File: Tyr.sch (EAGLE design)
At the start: 192 parts, among them J1 TYR_TYR_DISPLAY, U1 TYR_ATMEGA32U4, U2 CONTROLLER_PRTR5V0U2X, U4 TYR_TPS2552, X1 CONTROLLER_USB-C-12PUSB-C-12P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, Y1 16Mhz

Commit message: Initial
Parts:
- removed U1: TYR_ATMEGA32U4, Tyr:TYR_ATMEGA32U4
- added C45, C46: 22p, Tyr:COMPONENTS_CAPACITOR-0603
- added C47: 10n, Tyr:COMPONENTS_CAPACITOR-0603
- added C48: 1u, Tyr:COMPONENTS_CAPACITOR-0603
- added C49, C50, C51, C52, C54: 100n, Tyr:COMPONENTS_CAPACITOR-0603
- added C53: 4.7u, Tyr:COMPONENTS_CAPACITOR-0603
- added D42: 1N4148, Tyr:COMPONENTS_DIODE-SOD-123
- added D43: BAT60J, diode:BAT60J
- added U$1: STM32F303CC, Tyr:STM32F303CC
- added U$2: MCP1700T, Tyr:MCP1700T
- added Y2: 72Mhz, Tyr:CONTROLLER_CRYSTAL-4PIN-3.2X2.5
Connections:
- new net 3.3V: C47.1, C48.1, C50.1, C51.1, C52.1, C53.1, C54.2, D42.A, U$1.VBAT, U$1.VCC, U$1.VCC/VDDA/VREF+, U$1.VCC1, U$1.VCC2, U$2.VO
- new net BOOT0: U$1.BOOT0
- new net NRST: U$1.NRST
- net COLUMN0: no longer U1.PD4(ICP1/ADC8)
- net COLUMN1: no longer U1.PD6(T1/ADC9/!OC4D)
- net COLUMN2: no longer U1.PD7(OC4D/ADC10/T0)
- net COLUMN3: no longer U1.PB4(ADC11)
- net COLUMN4: no longer U1.PB5(OC1A/ADC12/!OC4B)
- net COLUMN5: no longer U1.PB6(OC1B/OC4B/ADC13)
- net COLUMN6: no longer U1.PC6(OC3A/!OC4A)
- net COLUMN7: no longer U1.PC7(ICP3/CLK0/OC4A)
- net D+: now also U$1.PA12/USB_DP; no longer U1.D+
- net D-: now also U$1.PA11/USB_DM; no longer U1.D-
- net GND: now also C45.1, C46.1, C47.2, C48.2, C49.1, C50.2, C51.2, C52.2, C53.2, C54.1, D43.A, U$1.GND, U$1.GND/VSSA/VREF-, U$1.GND1, U$1.GND2, U$2.GND, Y2.GND; no longer U1.GND, U1.GND1, U1.GND2, U1.GND3, U1.THERMAL, U1.UGND
- net LED_DATA: no longer U1.PD5(XCK/CTS)
- net LED_ENABLE: no longer U1.PD2(INT2/RXD1)
- net LED_FAULT: no longer U1.PD3(INT3/TXD1)
- net N$5: no longer U1.PE2(!HWB)
- net N$8: no longer U1.UCAP
- net RESET: no longer U1./RESET
- net ROW0: no longer U1.PF0(ADC0)
- net ROW1: no longer U1.PF1(ADC1)
- net ROW2: no longer U1.PF4(ADC4/TCK)
- net ROW3: no longer U1.PF5(ADC5/TMS)
- net ROW4: no longer U1.PF6(ADC6/TDO)
- net ROW5: no longer U1.PF7(ADC7(TDI)
- net SCL: now also U$1.I2C2_SCL/PA9; no longer U1.PD0(INT0/OC0B/SCL)
- net SDA: now also U$1.I2C2_SDA/PA10; no longer U1.PD1(INT1/SDA)
- net VCC: now also C49.2, D42.C, D43.C, U$2.VI; no longer U1.AVCC, U1.AVCC1, U1.UVCC, U1.VBUS, U1.VCC, U1.VCC1
- net XTAL1: now also C45.2, U$1.PF0/OSC_IN/12C2_SDA, Y2.1; no longer U1.XTAL1
- net XTAL2: now also C46.2, U$1.PF1/OSC_OUT/I2C2_SCL, Y2.2; no longer U1.XTAL2

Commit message: Layout
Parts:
- removed C3, C4: 0.1u, Tyr:COMPONENTS_CAPACITOR-0603
- removed C5: 4.7u, Tyr:COMPONENTS_CAPACITOR-0603
- removed C6, C7: 22p, Tyr:COMPONENTS_CAPACITOR-0603
- removed R3: 10k, Tyr:COMPONENTS_RESISTOR-0603
- removed Y1: 16Mhz, Tyr:CONTROLLER_CRYSTAL-4PIN-3.2X2.5
- added D45: 1N4148, Tyr:COMPONENTS_DIODE-SOD-123
- added U$3: DTC123J, Tyr:DTC123J
- C1: value 1u -> 4.7n
- C2: value 0.1u -> 10u
- R1: value 10k -> 100k
- Y2: value 72Mhz -> 8Mhz
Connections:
- removed net N$8: C1.2
- removed net RESET: R1.2, SJ1.2
- net 3.3V: now also SJ1.1
- net BOOT0: now also C2.2, D45.C, R1.1
- net GND: now also C1.2, R1.2, U$3.E; no longer C1.1, C3.1, C4.1, C5.1, C6.1, C7.1, R3.1, SJ1.1, Y1.GND
- net N$5: now also D45.A, SJ1.2, U$3.B; no longer R3.2
- net NRST: now also C1.1, U$3.C
- net VCC: no longer C2.2, C3.2, C4.2, C5.2, R1.1
- net XTAL1: no longer C6.2, Y1.1
- net XTAL2: no longer C7.2, Y1.2

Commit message: Update
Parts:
- removed 1, 2, 3, 4, 5, 6, A, ALT, B, C, CTRL, D, E, ESC, F, F1, F2, F3, F4, F5, F6, FN, G, GRAVE, H, HOME, INSERT, Q, R, S, T, TAB, V, W, WIN, X, Y, Z: KEYBOARD_KEYSWITCH-MX-1U-HOTSWAP, Tyr:KEYBOARD_KEYSWITCH-MX-1U-HOTSWAP
- removed C50, C51, C52, C54: 100n, Tyr:COMPONENTS_CAPACITOR-0603
- removed C53: 4.7u, Tyr:COMPONENTS_CAPACITOR-0603
- removed CAPSLOCK: KEYBOARD_KEYSWITCH-MX-1U-HOTSWAPCAPSLOCK, Tyr:KEYBOARD_KEYSWITCH-MX-1U-HOTSWAPCAPSLOCK
- removed D45: 1N4148, Tyr:COMPONENTS_DIODE-SOD-123
- removed R10: 5.1k, Tyr:COMPONENTS_RESISTOR-0603
- removed SHIFT, SPACE: KEYBOARD_KEYSWITCH-MX-2U-HOTSWAP, Tyr:KEYBOARD_KEYSWITCH-MX-2U-HOTSWAP
- removed SJ1: (no value), Tyr:MICROBUILDER_SOLDERJUMPER
- removed U$3: DTC123J, Tyr:DTC123J
- removed Y2: 8Mhz, Tyr:CONTROLLER_CRYSTAL-4PIN-3.2X2.5
- added C3: 4.7n, Tyr:COMPONENTS_CAPACITOR-0603
- added C4: 10u, Tyr:COMPONENTS_CAPACITOR-0603
- added C5: 22p, Tyr:COMPONENTS_CAPACITOR-0603
- added C6: 0.1u, Tyr:COMPONENTS_CAPACITOR-0603
- added C7: 10n, Tyr:COMPONENTS_CAPACITOR-0603
- added D44: 1N4148, Tyr:COMPONENTS_DIODE-SOD-123
- added KEYSWITCH1, KEYSWITCH10, KEYSWITCH11, KEYSWITCH12, KEYSWITCH13, KEYSWITCH14, KEYSWITCH15, KEYSWITCH16, KEYSWITCH17, KEYSWITCH18, KEYSWITCH19, KEYSWITCH2, KEYSWITCH20, KEYSWITCH21, KEYSWITCH22, KEYSWITCH23, KEYSWITCH24, KEYSWITCH25, KEYSWITCH26, KEYSWITCH27, KEYSWITCH28, KEYSWITCH29, KEYSWITCH3, KEYSWITCH30, KEYSWITCH31, KEYSWITCH32, KEYSWITCH33, KEYSWITCH34, KEYSWITCH35, KEYSWITCH36, KEYSWITCH37, KEYSWITCH38, KEYSWITCH39, KEYSWITCH5, KEYSWITCH6, KEYSWITCH7, KEYSWITCH8, KEYSWITCH9: KEYBOARD_KEYSWITCH-MX-1U-HOTSWAP, Tyr:KEYBOARD_KEYSWITCH-MX-1U-HOTSWAP
- added KEYSWITCH4: KEYBOARD_KEYSWITCH-MX-1U-HOTSWAPCAPSLOCK, Tyr:KEYBOARD_KEYSWITCH-MX-1U-HOTSWAPCAPSLOCK
- added Q1: DTC123J, Tyr:DTC123J
- added R3: 100k, Tyr:COMPONENTS_RESISTOR-0603
- added SWITCH1, SWITCH2: KEYBOARD_KEYSWITCH-MX-2U-HOTSWAP, Tyr:KEYBOARD_KEYSWITCH-MX-2U-HOTSWAP
- added U1: (no value), Tyr:MICROBUILDER_INA219
- added U5: MCP1700T, Tyr:MCP1700T
- added Y1: 8Mhz, Tyr:CONTROLLER_CRYSTAL-4PIN-3.2X2.5
- C1: value 4.7n -> 0.1u
- C10, C11, C13, C14: value 104 -> 100n
- C12: value 104 -> 4.7u
- C2: value 10u -> 22p
- C45, C46: value 22p -> 104
- C47: value 10n -> 104
- C48: value 1u -> 104
- C49: value 100n -> 104
- C8: value 0.1u -> 1u
- C9: value 0.1u -> 100n
- D2: value 1N4148 -> BAT60J; device Tyr:COMPONENTS_DIODE-SOD-123 -> diode:BAT60J
- D43: value BAT60J -> 1N4148; device diode:BAT60J -> Tyr:COMPONENTS_DIODE-SOD-123
- R2: value 22 -> 0.1/1% (PT2512FK-070R1L); device Tyr:COMPONENTS_RESISTOR-0603 -> Tyr:MICROBUILDER_RESISTOR2512
- R4: value 22 -> 10k
- R5: value 0.1/1% (PT2512FK-070R1L) -> 54.9k; device Tyr:MICROBUILDER_RESISTOR2512 -> Tyr:COMPONENTS_RESISTOR-0603
- R6: value 54.9k -> 22
- R7: value 10k -> 22
- R8: value 100k -> 5.1k
- U$1: value STM32F303CC -> BUTTON; device Tyr:STM32F303CC -> Tyr:BUTTON
- U$2: value MCP1700T -> PINHEADER_1X6; device Tyr:MCP1700T -> Tyr:PINHEADER_1X6
- U2: value CONTROLLER_PRTR5V0U2X -> STM32F303CC; device Tyr:CONTROLLER_PRTR5V0U2X -> Tyr:STM32F303CC
- U3: value (none) -> TYR_TPS2552; device Tyr:MICROBUILDER_INA219 -> Tyr:TYR_TPS2552
- U4: value TYR_TPS2552 -> CONTROLLER_PRTR5V0U2X; device Tyr:TYR_TPS2552 -> Tyr:CONTROLLER_PRTR5V0U2X
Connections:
- new net SWCLK: U$2.5, U2.PA14/SWCLK-JTCK/I2C1_SDA
- new net SWDIO: U$2.4, U2.PA13/SWDIO-JTMS
- net 3.3V: now also C10.1, C11.1, C12.1, C14.2, C7.1, C8.1, C9.1, D3.A, J1.4, U$1.P$2, U$2.6, U2.VBAT, U2.VCC, U2.VCC/VDDA/VREF+, U2.VCC1, U2.VCC2, U5.VO; no longer C47.1, C48.1, C50.1, C51.1, C52.1, C53.1, C54.2, D42.A, SJ1.1, U$1.VBAT, U$1.VCC, U$1.VCC/VDDA/VREF+, U$1.VCC1, U$1.VCC2, U$2.VO
- net BOOT0: now also C4.2, D1.C, U$2.3, U2.BOOT0; no longer C2.2, D45.C, U$1.BOOT0
- net COLUMN0: now also KEYSWITCH1.P1, KEYSWITCH2.P1, KEYSWITCH3.P1, KEYSWITCH4.P1, KEYSWITCH5.P1, SWITCH1.P1, U2.DAC1-OUT2/PA5; no longer CAPSLOCK.P1, CTRL.P1, ESC.P1, GRAVE.P1, SHIFT.P1, TAB.P1
- net COLUMN1: now also KEYSWITCH10.P1, KEYSWITCH11.P1, KEYSWITCH6.P1, KEYSWITCH7.P1, KEYSWITCH8.P1, KEYSWITCH9.P1, U2.PA6; no longer 1.P1, A.P1, F1.P1, Q.P1, WIN.P1, Z.P1
- net COLUMN2: now also KEYSWITCH12.P1, KEYSWITCH13.P1, KEYSWITCH14.P1, KEYSWITCH15.P1, KEYSWITCH16.P1, KEYSWITCH17.P1, U2.PA7; no longer 2.P1, ALT.P1, F2.P1, S.P1, W.P1, X.P1
- net COLUMN3: now also KEYSWITCH18.P1, KEYSWITCH19.P1, KEYSWITCH20.P1, KEYSWITCH21.P1, KEYSWITCH22.P1, SWITCH2.P1, U2.PB0; no longer 3.P1, C.P1, D.P1, E.P1, F3.P1, SPACE.P1
- net COLUMN4: now also KEYSWITCH23.P1, KEYSWITCH24.P1, KEYSWITCH25.P1, KEYSWITCH26.P1, KEYSWITCH27.P1, U2.PB1; no longer 4.P1, F.P1, F4.P1, R.P1, V.P1
- net COLUMN5: now also KEYSWITCH28.P1, KEYSWITCH29.P1, KEYSWITCH30.P1, KEYSWITCH31.P1, KEYSWITCH32.P1, KEYSWITCH33.P1, U2.PB10; no longer 5.P1, B.P1, F5.P1, FN.P1, G.P1, T.P1
- net COLUMN6: now also KEYSWITCH34.P1, KEYSWITCH35.P1, U2.PB11; no longer 6.P1, F6.P1
- net COLUMN7: now also KEYSWITCH36.P1, KEYSWITCH37.P1, KEYSWITCH38.P1, KEYSWITCH39.P1, U2.PB12; no longer H.P1, HOME.P1, INSERT.P1, Y.P1
- net D+: now also R7.2, U2.PA12/USB_DP; no longer R4.2, U$1.PA12/USB_DP
- net D-: now also R6.2, U2.PA11/USB_DM; no longer R2.2, U$1.PA11/USB_DM
- net GND: now also C1.1, C10.2, C11.2, C12.2, C3.2, C4.1, C47.1, C48.1, C5.1, C6.1, C7.2, C8.2, C9.2, D2.A, KEYSWITCH1.HOLE, KEYSWITCH10.HOLE, KEYSWITCH11.HOLE, KEYSWITCH12.HOLE, KEYSWITCH13.HOLE, KEYSWITCH14.HOLE, KEYSWITCH15.HOLE, KEYSWITCH16.HOLE, KEYSWITCH17.HOLE, KEYSWITCH18.HOLE, KEYSWITCH19.HOLE, KEYSWITCH2.HOLE, KEYSWITCH20.HOLE, KEYSWITCH21.HOLE, KEYSWITCH22.HOLE, KEYSWITCH23.HOLE, KEYSWITCH24.HOLE, KEYSWITCH25.HOLE, KEYSWITCH26.HOLE, KEYSWITCH27.HOLE, KEYSWITCH28.HOLE, KEYSWITCH29.HOLE, KEYSWITCH3.HOLE, KEYSWITCH30.HOLE, KEYSWITCH31.HOLE, KEYSWITCH32.HOLE, KEYSWITCH33.HOLE, KEYSWITCH34.HOLE, KEYSWITCH35.HOLE, KEYSWITCH36.HOLE, KEYSWITCH37.HOLE, KEYSWITCH38.HOLE, KEYSWITCH39.HOLE, KEYSWITCH4.HOLE, KEYSWITCH5.HOLE, KEYSWITCH6.HOLE, KEYSWITCH7.HOLE, KEYSWITCH8.HOLE, KEYSWITCH9.HOLE, Q1.E, R4.1, R5.1, R8.2, SWITCH1.HOLE, SWITCH2.HOLE, U$2.1, U1.GND, U2.GND, U2.GND/VSSA/VREF-, U2.GND1, U2.GND2, U4.1, U5.GND, Y1.GND; no longer 1.HOLE, 2.HOLE, 3.HOLE, 4.HOLE, 5.HOLE, 6.HOLE, A.HOLE, ALT.HOLE, B.HOLE, C.HOLE, C1.2, C10.1, C11.1, C12.1, C47.2, C48.2, C50.2, C51.2, C52.2, C53.2, C54.1, C8.1, C9.1, CAPSLOCK.HOLE, CTRL.HOLE, D.HOLE, D43.A, E.HOLE, ESC.HOLE, F.HOLE, F1.HOLE, F2.HOLE, F3.HOLE, F4.HOLE, F5.HOLE, F6.HOLE, FN.HOLE, G.HOLE, GRAVE.HOLE, H.HOLE, HOME.HOLE, INSERT.HOLE, Q.HOLE, R.HOLE, R10.2, R6.1, R7.1, S.HOLE, SHIFT.HOLE, SPACE.HOLE, T.HOLE, TAB.HOLE, U$1.GND, U$1.GND/VSSA/VREF-, U$1.GND1, U$1.GND2, U$2.GND, U$3.E, U2.1, U4.GND, V.HOLE, W.HOLE, WIN.HOLE, X.HOLE, Y.HOLE, Y2.GND, Z.HOLE
- net LED_DATA: now also LED35.DI, U2.DAC1-OUT1/PA4; no longer LED41.DI
- net LED_ENABLE: now also R4.2, U2.PA1, U3.EN; no longer R7.2, U4.EN
- net LED_FAULT: now also R3.1, U2.PA2, U3.FAULT; no longer R8.1, U4.FAULT
- net LED_VCC: now also C45.2, C46.2, C47.2, C48.2, C49.2, U3.OUT; no longer C10.2, C11.2, C12.2, C13.2, C14.2, U4.OUT
- net N$1: now also D11.A, KEYSWITCH7.P0; no longer 1.P0, D10.A
- net N$10: now also D4.A, KEYSWITCH1.P0; no longer D1.A, ESC.P0
- net N$11: now also D10.A, KEYSWITCH6.P0; no longer D2.A, F1.P0
- net N$12: now also D16.A, KEYSWITCH12.P0; no longer D3.A, F2.P0
- net N$13: now also D22.A, KEYSWITCH18.P0; no longer D4.A, F3.P0
- net N$14: now also D28.A, KEYSWITCH23.P0; no longer D5.A, F4.P0
- net N$15: now also D33.A, KEYSWITCH28.P0; no longer D6.A, F5.P0
- net N$16: now also D39.A, KEYSWITCH34.P0; no longer D7.A, F6.P0
- net N$17: now also D41.A, KEYSWITCH36.P0; no longer D8.A, HOME.P0
- net N$18: now also D42.A, KEYSWITCH37.P0; no longer D16.A, INSERT.P0
- net N$19: now also D40.A, KEYSWITCH35.P0; no longer 6.P0, D15.A
- net N$2: now also R2.2, U1.VIN-, U3.IN; no longer R5.2, U3.VIN-, U4.IN
- net N$20: now also D34.A, KEYSWITCH29.P0; no longer 5.P0, D14.A
- net N$21: now also D29.A, KEYSWITCH24.P0; no longer 4.P0, D13.A
- net N$22: now also D23.A, KEYSWITCH19.P0; no longer 3.P0, D12.A
- net N$23: now also D17.A, KEYSWITCH13.P0; no longer 2.P0, D11.A
- net N$24: now also D5.A, KEYSWITCH2.P0; no longer D9.A, GRAVE.P0
- net N$25: now also D43.A, KEYSWITCH38.P0; no longer D23.A, Y.P0
- net N$26: now also D35.A, KEYSWITCH30.P0; no longer D22.A, T.P0
- net N$27: now also D30.A, KEYSWITCH25.P0; no longer D21.A, R.P0
- net N$28: now also D24.A, KEYSWITCH20.P0; no longer D20.A, E.P0
- net N$29: now also D18.A, KEYSWITCH14.P0; no longer D19.A, W.P0
- net N$3: now also R5.2, U3.ILIM; no longer R6.2, U4.ILIM
- net N$30: now also LED18.DI, LED24.DO; no longer LED39.DI, LED40.DO
- net N$31: now also D6.A, KEYSWITCH3.P0; no longer D17.A, TAB.P0
- net N$32: now also D7.A, KEYSWITCH4.P0; no longer CAPSLOCK.P0, D24.A
- net N$33: now also D13.A, KEYSWITCH9.P0; no longer A.P0, D25.A
- net N$34: now also D19.A, KEYSWITCH15.P0; no longer D26.A, S.P0
- net N$35: now also D25.A, KEYSWITCH21.P0; no longer D.P0, D27.A
- net N$36: now also D31.A, KEYSWITCH26.P0; no longer D28.A, F.P0
- net N$37: now also D36.A, KEYSWITCH31.P0; no longer D29.A, G.P0
- net N$38: now also D44.A, KEYSWITCH39.P0; no longer D30.A, H.P0
- net N$39: now also D37.A, KEYSWITCH32.P0; no longer B.P0, D36.A
- net N$4: now also R8.1; no longer R9.1
- net N$40: now also D26.A, KEYSWITCH22.P0; no longer C.P0, D34.A
- net N$41: now also D20.A, KEYSWITCH16.P0; no longer D33.A, X.P0
- net N$42: now also D14.A, KEYSWITCH10.P0; no longer D32.A, Z.P0
- net N$43: now also D8.A, SWITCH1.P0; no longer D31.A, SHIFT.P0
- net N$44: now also D9.A, KEYSWITCH5.P0; no longer CTRL.P0, D37.A
- net N$45: now also D15.A, KEYSWITCH11.P0; no longer D38.A, WIN.P0
- net N$46: now also D21.A, KEYSWITCH17.P0; no longer ALT.P0, D39.A
- net N$47: now also D27.A, SWITCH2.P0; no longer D40.A, SPACE.P0
- net N$48: now also D38.A, KEYSWITCH33.P0; no longer D41.A, FN.P0
- net N$49: now also D32.A, KEYSWITCH27.P0; no longer D35.A, V.P0
- net N$5: now also D1.A, Q1.B, U$1.P$1; no longer D45.A, SJ1.2, U$3.B
- net N$50: now also D12.A, KEYSWITCH8.P0; no longer D18.A, Q.P0
- net N$51: now also LED12.DI, LED18.DO; no longer LED38.DI, LED39.DO
- net N$52: now also LED12.DO, LED6.DI; no longer LED37.DI, LED38.DO
- net N$53: now also LED34.DI, LED6.DO; no longer LED36.DI, LED37.DO
- net N$54: now also LED29.DI, LED34.DO; no longer LED35.DI, LED36.DO
- net N$55: now also LED23.DI, LED29.DO; no longer LED34.DI, LED35.DO
- net N$56: now also LED17.DI, LED23.DO; no longer LED33.DI, LED34.DO
- net N$57: now also LED11.DI, LED17.DO; no longer LED32.DI, LED33.DO
- net N$58: now also LED11.DO, LED5.DI; no longer LED31.DI, LED32.DO
- net N$59: now also LED41.DI, LED5.DO; no longer LED30.DI, LED31.DO
- net N$6: now also R6.1, U4.3; no longer R2.1, U2.3
- net N$60: now also LED33.DI, LED41.DO; no longer LED29.DI, LED30.DO
- net N$61: now also LED33.DO; no longer LED29.DO
- net N$62: now also LED22.DI; no longer LED27.DI
- net N$63: now also LED16.DI, LED22.DO; no longer LED26.DI, LED27.DO
- net N$64: now also LED10.DI, LED16.DO; no longer LED25.DI, LED26.DO
- net N$65: now also LED10.DO, LED4.DI; no longer LED24.DI, LED25.DO
- net N$66: now also LED4.DO, LED40.DI; no longer LED23.DI, LED24.DO
- net N$67: now also LED32.DI, LED40.DO; no longer LED22.DI, LED23.DO
- net N$68: now also LED27.DI, LED32.DO; no longer LED21.DI, LED22.DO
- net N$69: now also LED21.DI, LED27.DO; no longer LED20.DI, LED21.DO
- net N$7: now also R7.1, U4.2; no longer R4.1, U2.2
- net N$70: now also LED15.DI, LED21.DO; no longer LED19.DI, LED20.DO
- net N$71: now also LED15.DO, LED9.DI; no longer LED18.DI, LED19.DO
- net N$72: now also LED3.DI, LED9.DO; no longer LED17.DI, LED18.DO
- net N$73: now also LED3.DO, LED39.DI; no longer LED16.DI, LED17.DO
- net N$74: now also LED37.DI, LED39.DO; no longer LED15.DI, LED16.DO
- net N$75: now also LED31.DI, LED37.DO; no longer LED14.DI, LED15.DO
- net N$76: now also LED26.DI, LED31.DO; no longer LED13.DI, LED14.DO
- net N$77: now also LED20.DI, LED26.DO; no longer LED12.DI, LED13.DO
- net N$78: now also LED14.DI, LED20.DO; no longer LED11.DI, LED12.DO
- net N$79: now also LED14.DO, LED8.DI; no longer LED10.DI, LED11.DO
- net N$80: now also LED2.DI, LED8.DO; no longer LED10.DO, LED9.DI
- net N$81: now also LED2.DO, LED38.DI; no longer LED8.DI, LED9.DO
- net N$82: now also LED36.DI, LED38.DO; no longer LED7.DI, LED8.DO
- net N$83: now also LED30.DI, LED36.DO; no longer LED6.DI, LED7.DO
- net N$84: now also LED25.DI, LED30.DO; no longer LED5.DI, LED6.DO
- net N$85: now also LED19.DI, LED25.DO; no longer LED4.DI, LED5.DO
- net N$86: now also LED13.DI, LED19.DO; no longer LED3.DI, LED4.DO
- net N$87: now also LED13.DO, LED7.DI; no longer LED2.DI, LED3.DO
- net N$88: now also LED7.DO; no longer LED2.DO
- net N$89: now also R9.1; no longer R10.1
- net N$9: now also LED24.DI, LED35.DO; no longer LED40.DI, LED41.DO
- net NRST: now also C3.1, Q1.C, U$2.2, U2.NRST; no longer C1.1, U$1.NRST, U$3.C
- net ROW0: now also D10.C, D16.C, D22.C, D28.C, D33.C, D39.C, D41.C, U2.PA8; no longer D1.C, D2.C, D3.C, D5.C, D6.C, D7.C, D8.C
- net ROW1: now also D17.C, D23.C, D29.C, D34.C, D40.C, D42.C, D5.C, U2.PB15; no longer D10.C, D12.C, D13.C, D14.C, D15.C, D16.C, D9.C
- net ROW2: now also D12.C, D24.C, D30.C, D35.C, D43.C, D6.C, U2.PB14; no longer D17.C, D19.C, D20.C, D21.C, D22.C, D23.C
- net ROW3: now also D13.C, D19.C, D31.C, D36.C, D44.C, D7.C, U2.PB13; no longer D24.C, D26.C, D27.C, D28.C, D29.C, D30.C
- net ROW4: now also D14.C, D20.C, D26.C, D37.C, D8.C, U2.PB2; no longer D31.C, D33.C, D34.C, D35.C, D36.C
- net ROW5: now also D15.C, D21.C, D27.C, D9.C, U2.PA3; no longer D37.C, D39.C, D40.C, D41.C
- net SCL: now also U1.SCL, U2.I2C2_SCL/PA9; no longer U$1.I2C2_SCL/PA9, U3.SCL
- net SDA: now also U1.SDA, U2.I2C2_SDA/PA10; no longer U$1.I2C2_SDA/PA10, U3.SDA
- net VCC: now also C1.2, C13.2, C6.2, D2.C, D3.C, R2.1, R3.2, U1.VCC, U1.VIN+, U4.4, U5.VI; no longer C49.2, C8.2, C9.2, D42.C, D43.C, J1.4, R5.1, R8.2, U$2.VI, U2.4, U3.VCC, U3.VIN+
- net XTAL1: now also C2.2, U2.PF0/OSC_IN/12C2_SDA, Y1.1; no longer C45.2, U$1.PF0/OSC_IN/12C2_SDA, Y2.1
- net XTAL2: now also C5.2, U2.PF1/OSC_OUT/I2C2_SCL, Y1.2; no longer C46.2, U$1.PF1/OSC_OUT/I2C2_SCL, Y2.2

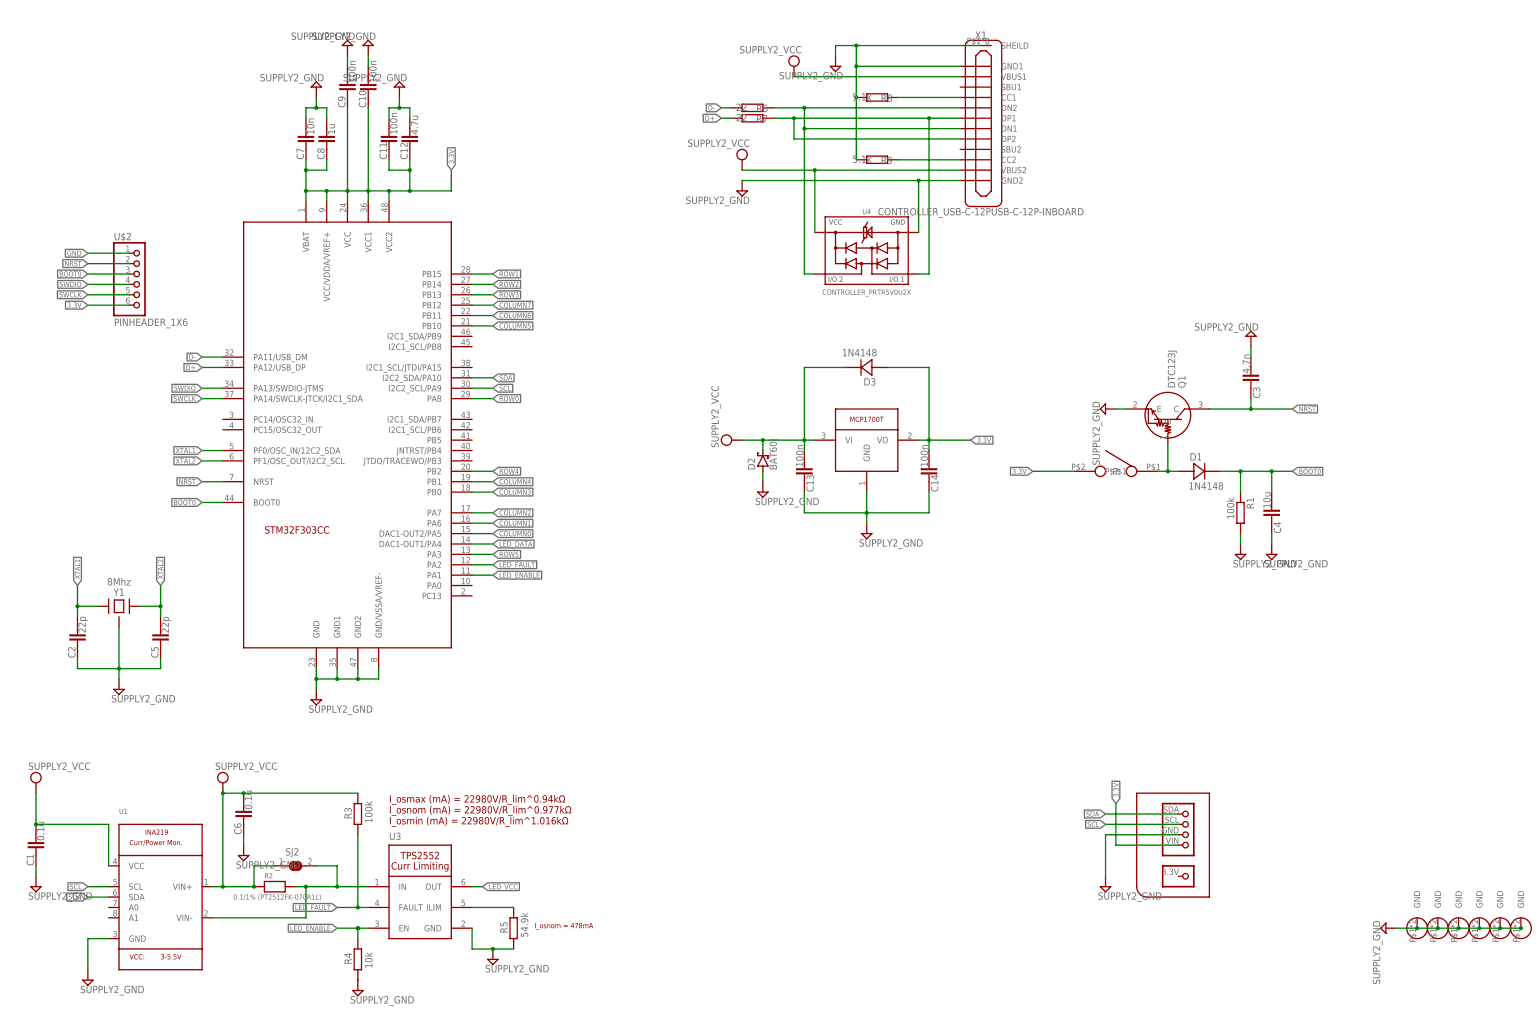
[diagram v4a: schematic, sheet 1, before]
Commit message: Fix current monitoring & added I2C FRAM
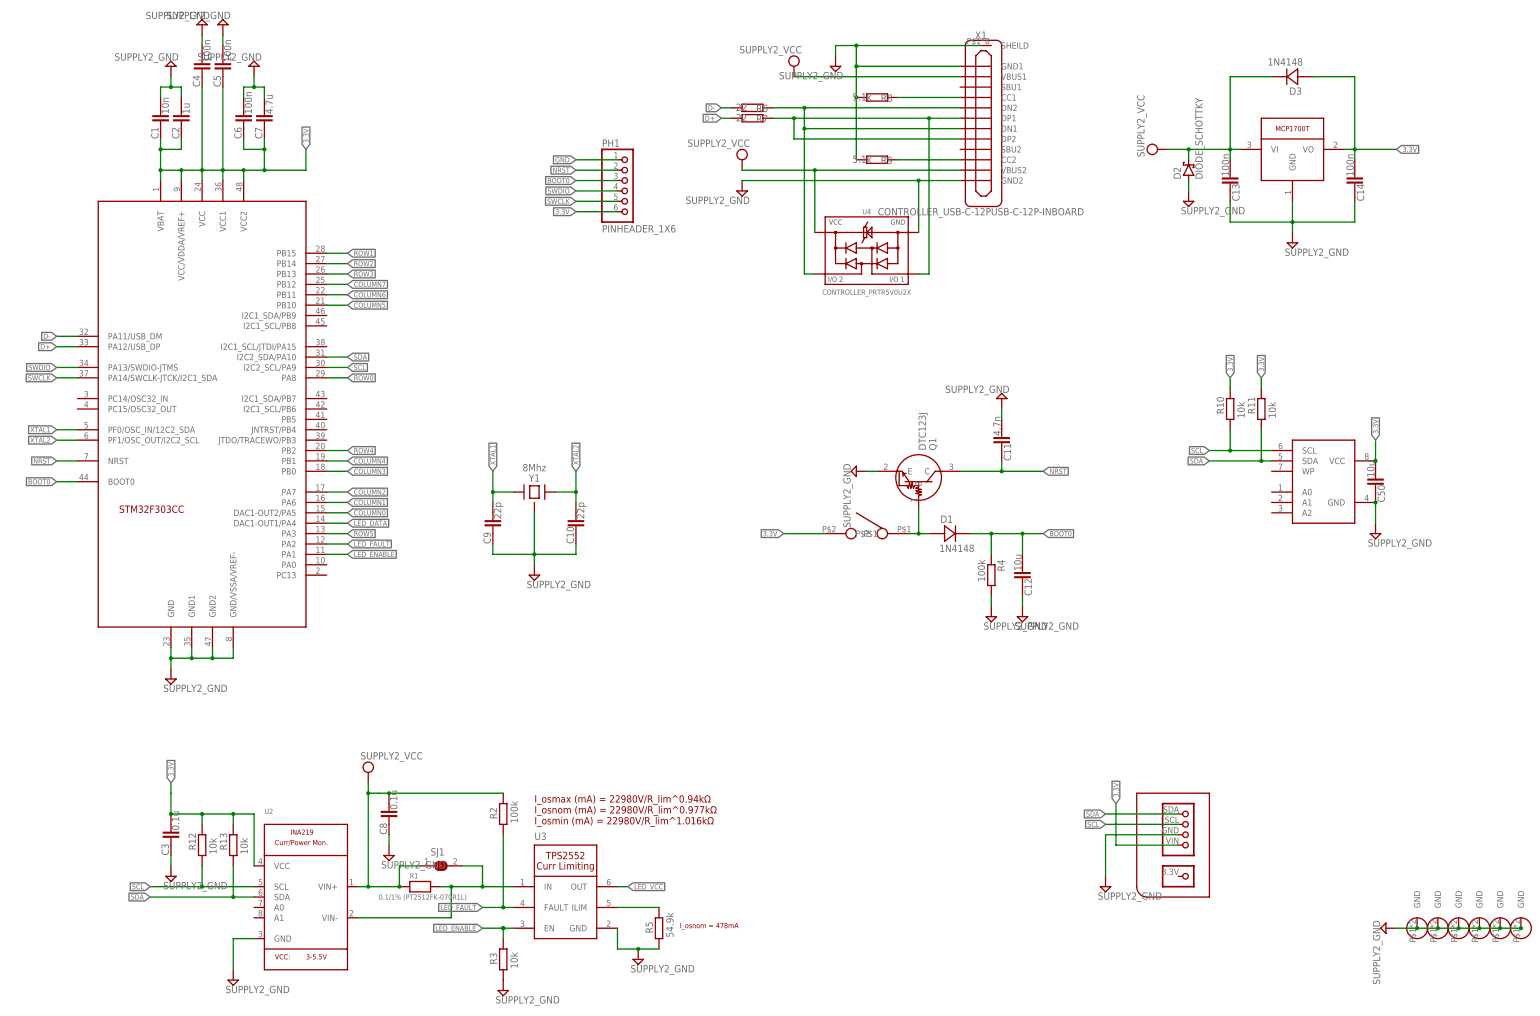
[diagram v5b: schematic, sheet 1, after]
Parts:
- removed SJ2: (no value), Tyr:MICROBUILDER_SOLDERJUMPER
- removed U$2: PINHEADER_1X6, Tyr:PINHEADER_1X6
- added C50: 10u, Tyr:COMPONENTS_CAPACITOR-0603
- added PH1: PINHEADER_1X6, Tyr:PINHEADER_1X6
- added R10, R11, R12, R13: 10k, Tyr:COMPONENTS_RESISTOR-0603
- added SJ1: (no value), Tyr:MICROBUILDER_SOLDERJUMPER
- added SW1: BUTTON, Tyr:BUTTON
- C1: value 0.1u -> 10n
- C10, C9: value 100n -> 22p
- C11: value 100n -> 4.7n
- C12: value 4.7u -> 10u
- C2: value 22p -> 1u
- C3: value 4.7n -> 0.1u
- C4: value 10u -> 100n
- C5: value 22p -> 100n
- C6: value 0.1u -> 100n
- C7: value 10n -> 4.7u
- C8: value 1u -> 0.1u
- D2: value BAT60J -> DIODE_SCHOTTKY; device diode:BAT60J -> Tyr:DIODE_SCHOTTKY
- R1: value 100k -> 0.1/1% (PT2512FK-070R1L); device Tyr:COMPONENTS_RESISTOR-0603 -> Tyr:MICROBUILDER_RESISTOR2512
- R2: value 0.1/1% (PT2512FK-070R1L) -> 100k; device Tyr:MICROBUILDER_RESISTOR2512 -> Tyr:COMPONENTS_RESISTOR-0603
- R3: value 100k -> 10k
- R4: value 10k -> 100k
- U$1: value BUTTON -> MB85RC256V; device Tyr:BUTTON -> Tyr:MB85RC256V
- U1: value (none) -> STM32F303CC; device Tyr:MICROBUILDER_INA219 -> Tyr:STM32F303CC
- U2: value STM32F303CC -> (none); device Tyr:STM32F303CC -> Tyr:MICROBUILDER_INA219
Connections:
- net 3.3V: now also C1.1, C2.1, C3.2, C4.1, C5.1, C50.2, C6.1, PH1.6, R10.2, R11.2, R12.2, R13.2, SW1.P$2, U$1.VCC, U1.VBAT, U1.VCC, U1.VCC/VDDA/VREF+, U1.VCC1, U1.VCC2; no longer C10.1, C11.1, C12.1, C8.1, C9.1, U$1.P$2, U$2.6, U2.VBAT, U2.VCC/VDDA/VREF+, U2.VCC1, U2.VCC2
- net BOOT0: now also C12.2, PH1.3, R4.1, U1.BOOT0; no longer C4.2, R1.1, U$2.3, U2.BOOT0
- net COLUMN0: now also U1.DAC1-OUT2/PA5; no longer U2.DAC1-OUT2/PA5
- net COLUMN1: now also U1.PA6; no longer U2.PA6
- net COLUMN2: now also U1.PA7; no longer U2.PA7
- net COLUMN3: now also U1.PB0; no longer U2.PB0
- net COLUMN4: now also U1.PB1; no longer U2.PB1
- net COLUMN5: now also U1.PB10; no longer U2.PB10
- net COLUMN6: now also U1.PB11; no longer U2.PB11
- net COLUMN7: now also U1.PB12; no longer U2.PB12
- net D+: now also U1.PA12/USB_DP; no longer U2.PA12/USB_DP
- net D-: now also U1.PA11/USB_DM; no longer U2.PA11/USB_DM
- net GND: now also C1.2, C10.1, C12.1, C2.2, C3.1, C4.2, C5.2, C50.1, C6.2, C8.1, C9.1, PH1.1, R3.1, R4.2, U$1.GND, U1.GND/VSSA/VREF-, U1.GND1, U1.GND2; no longer C1.1, C10.2, C12.2, C2.1, C3.2, C4.1, C5.1, C6.1, C8.2, C9.2, R1.2, R4.1, U$2.1, U2.GND/VSSA/VREF-, U2.GND1, U2.GND2
- net LED_DATA: now also U1.DAC1-OUT1/PA4; no longer U2.DAC1-OUT1/PA4
- net LED_ENABLE: now also R3.2, U1.PA1; no longer R4.2, U2.PA1
- net LED_FAULT: now also R2.1, U1.PA2; no longer R3.1, U2.PA2
- net N$2: now also R1.2, SJ1.2, U2.VIN-; no longer R2.2, SJ2.2, U1.VIN-
- net N$5: now also SW1.P$1; no longer U$1.P$1
- net NRST: now also C11.1, PH1.2, U1.NRST; no longer C3.1, U$2.2, U2.NRST
- net ROW0: now also U1.PA8; no longer U2.PA8
- net ROW1: now also U1.PB15; no longer U2.PB15
- net ROW2: now also U1.PB14; no longer U2.PB14
- net ROW3: now also U1.PB13; no longer U2.PB13
- net ROW4: now also U1.PB2; no longer U2.PB2
- net ROW5: now also U1.PA3; no longer U2.PA3
- net SCL: now also R10.1, R12.1, U$1.SCL, U1.I2C2_SCL/PA9, U2.SCL; no longer U1.SCL, U2.I2C2_SCL/PA9
- net SDA: now also R11.1, R13.1, U$1.SDA, U1.I2C2_SDA/PA10, U2.SDA; no longer U1.SDA, U2.I2C2_SDA/PA10
- net SWCLK: now also PH1.5, U1.PA14/SWCLK-JTCK/I2C1_SDA; no longer U$2.5, U2.PA14/SWCLK-JTCK/I2C1_SDA
- net SWDIO: now also PH1.4, U1.PA13/SWDIO-JTMS; no longer U$2.4, U2.PA13/SWDIO-JTMS
- net VCC: now also C8.2, R1.1, R2.2, SJ1.1, U2.VIN+; no longer C1.2, C6.2, R2.1, R3.2, SJ2.1, U1.VCC, U1.VIN+
- net XTAL1: now also C9.2, U1.PF0/OSC_IN/12C2_SDA; no longer C2.2, U2.PF0/OSC_IN/12C2_SDA
- net XTAL2: now also C10.2, U1.PF1/OSC_OUT/I2C2_SCL; no longer C5.2, U2.PF1/OSC_OUT/I2C2_SCL
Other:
- moved on the sheet: C1, C10, C11, C12, C13, C14, C2, C3, C4, C5, C6, C7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
